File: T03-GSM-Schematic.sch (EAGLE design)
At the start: 24 parts, among them IC1 788TV, J1 POWER_JACKPTH_BREAD, J2 AVR, Q2 16M, U1 ATMEGA328P-PU

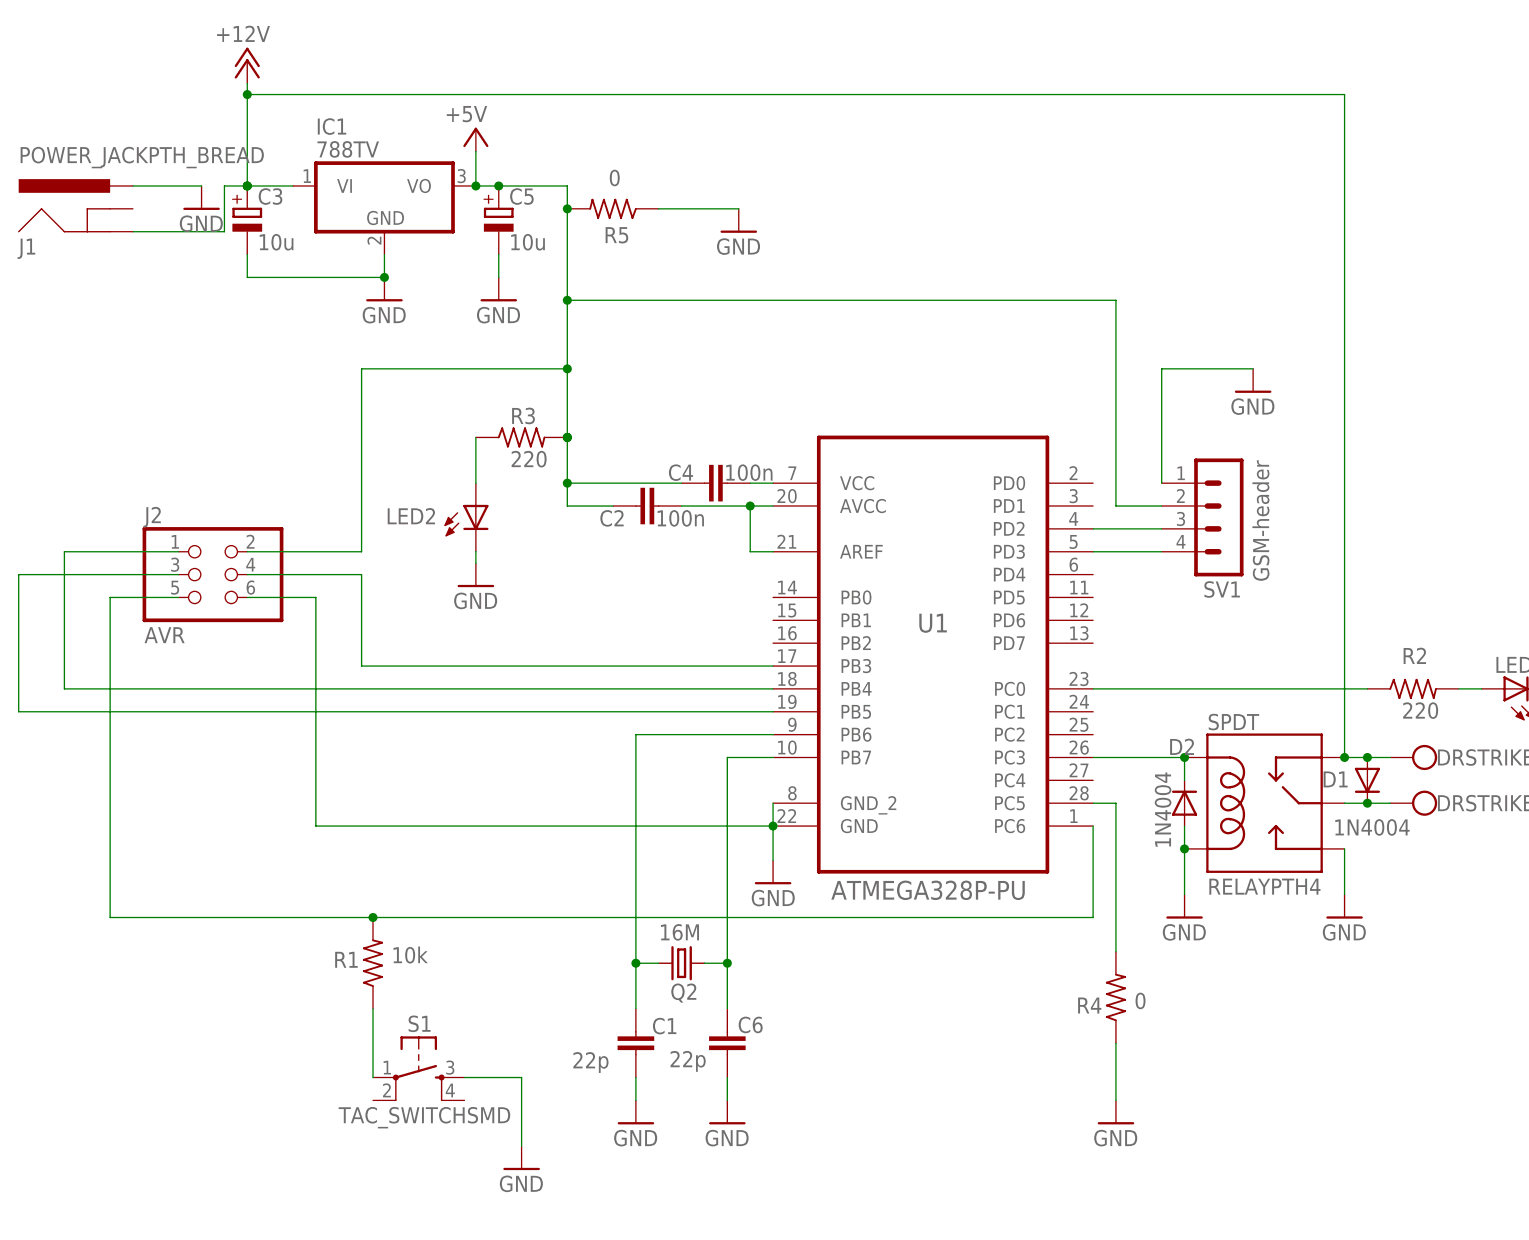
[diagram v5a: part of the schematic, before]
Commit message: Add files via upload
Final Revision. 
No DRC or ERC errors.
Updates:
Power lines thickened
Power capacitor orientation fixed
Reset pull-up resistor added
Power symbols used in schematic
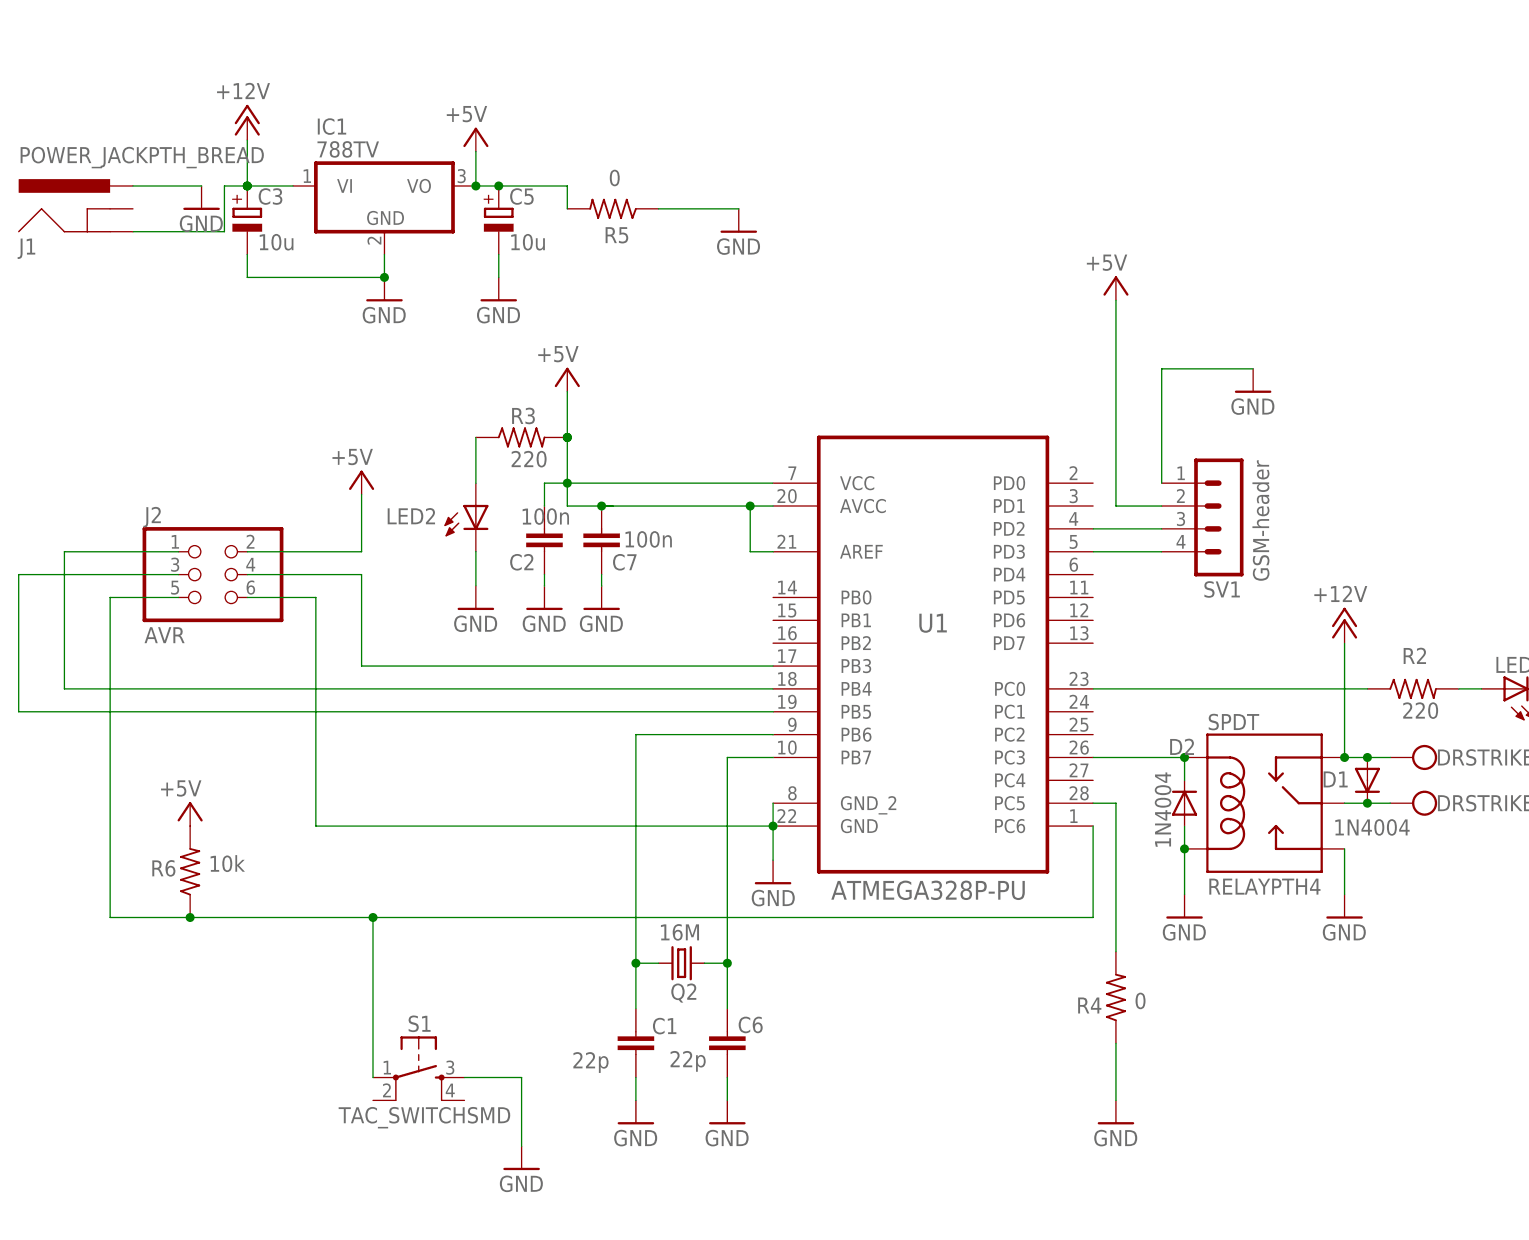
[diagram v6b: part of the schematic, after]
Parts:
- removed C4: 100n, rcl:C-EUC0603
- removed R1: 10k, rcl:R-US_R0603
- added C7: 100n, rcl:C-EUC0603
- added R6: 10k, rcl:R-US_R0603
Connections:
- removed net N$1: C2.2, U1.AREF, U1.AVCC
- removed net N$10: J2.5, R1.2, U1.PC6
- removed net N$11: C4.2, U1.VCC
- net +5V: now also C2.2, C7.2, R6.2, U1.AREF, U1.AVCC, U1.VCC; no longer C2.1, C4.1
- net GND: now also C2.1, C7.1
- net N$2: now also J2.5, R6.1, U1.PC6; no longer R1.1
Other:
- moved on the sheet: C2
